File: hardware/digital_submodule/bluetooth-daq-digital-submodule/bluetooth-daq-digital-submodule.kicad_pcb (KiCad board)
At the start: 2 copper layers, 148 parts, among them J1 MCU I/F, J2 Digital Inputs, J3 Digital Outputs, J4 Communication I/F, J5 RS-485 I/F, U1 74HC595, U2 74HC595, U3 74HC165, U4 74HC165, U5 24LC1025, U6 SN75176AD, U7 CD4053B, U8 CD4053B

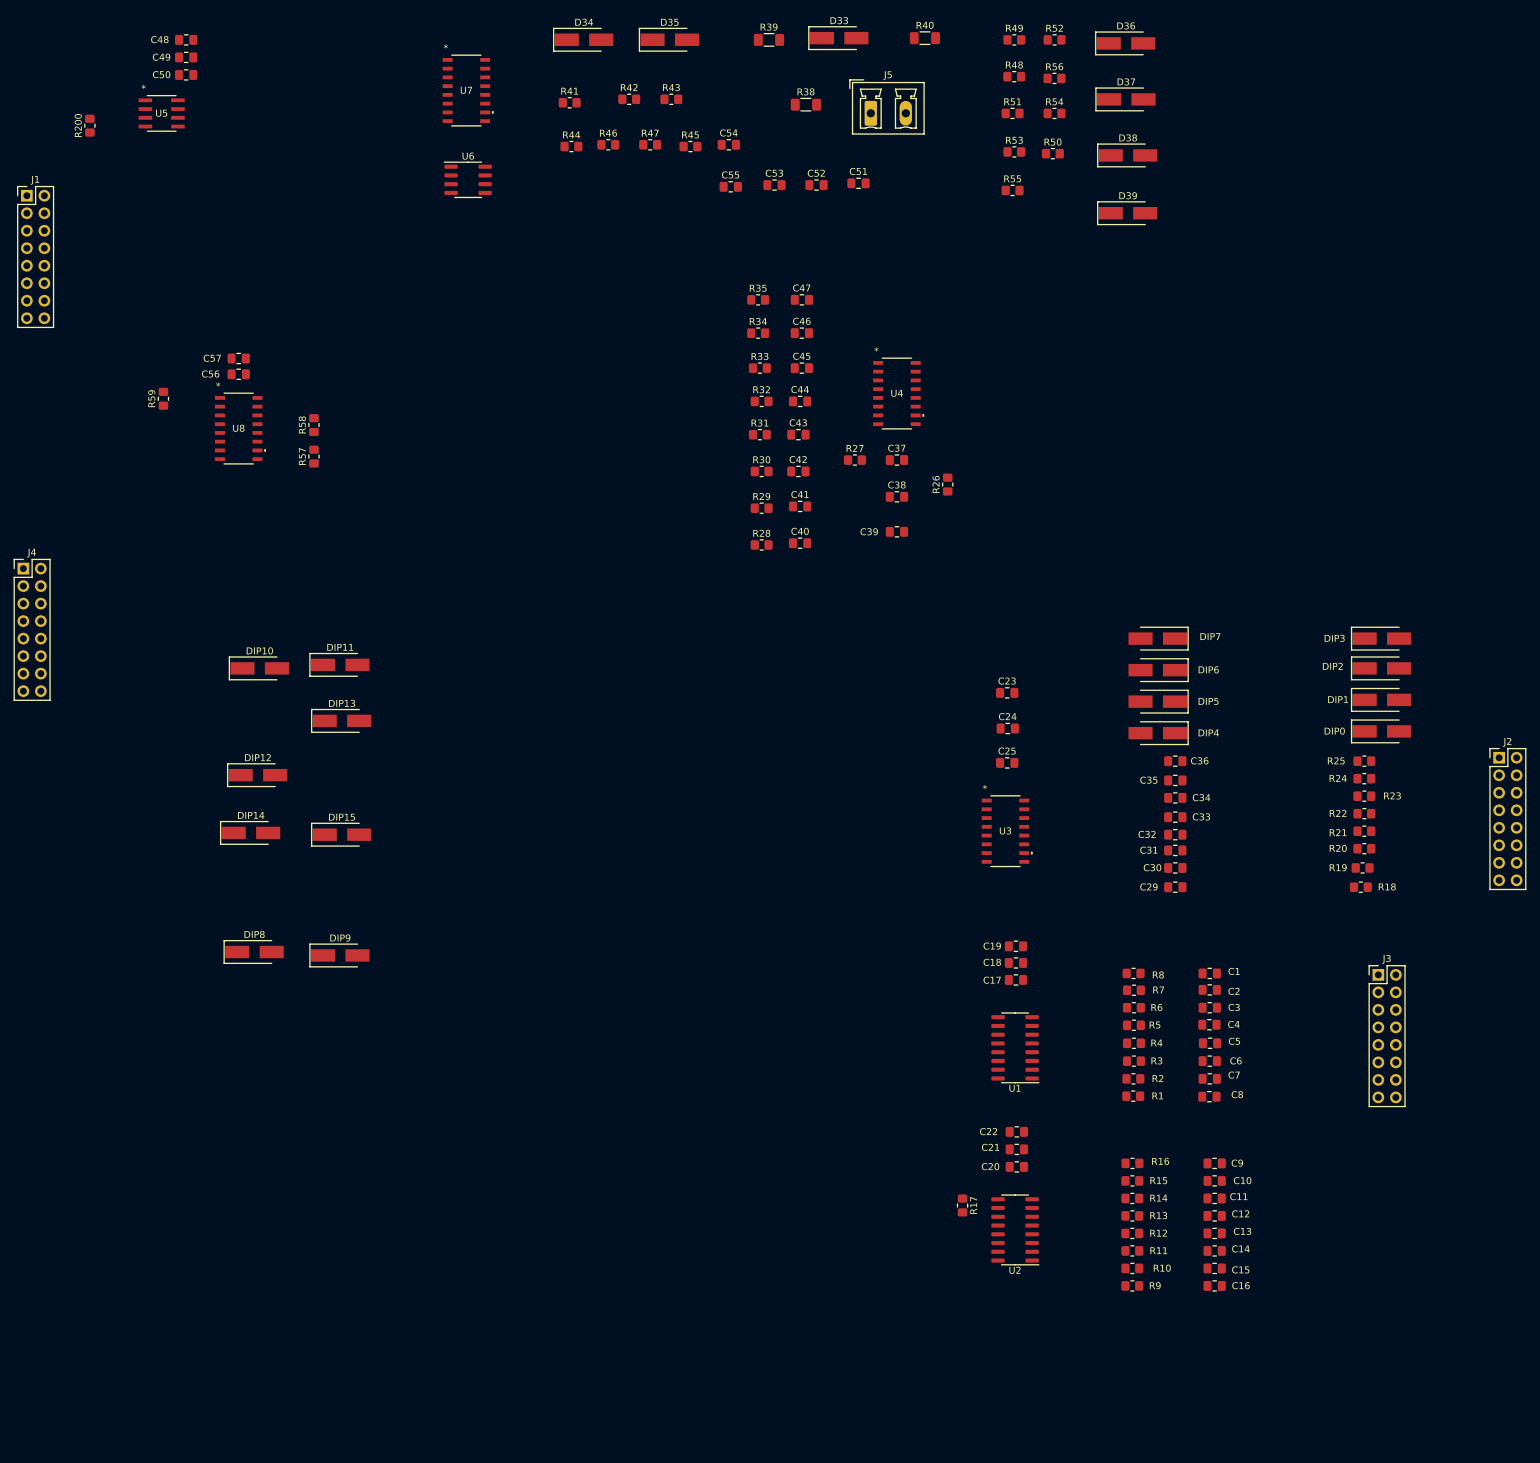
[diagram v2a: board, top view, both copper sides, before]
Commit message: Decided on initial component placement for digital submodule.
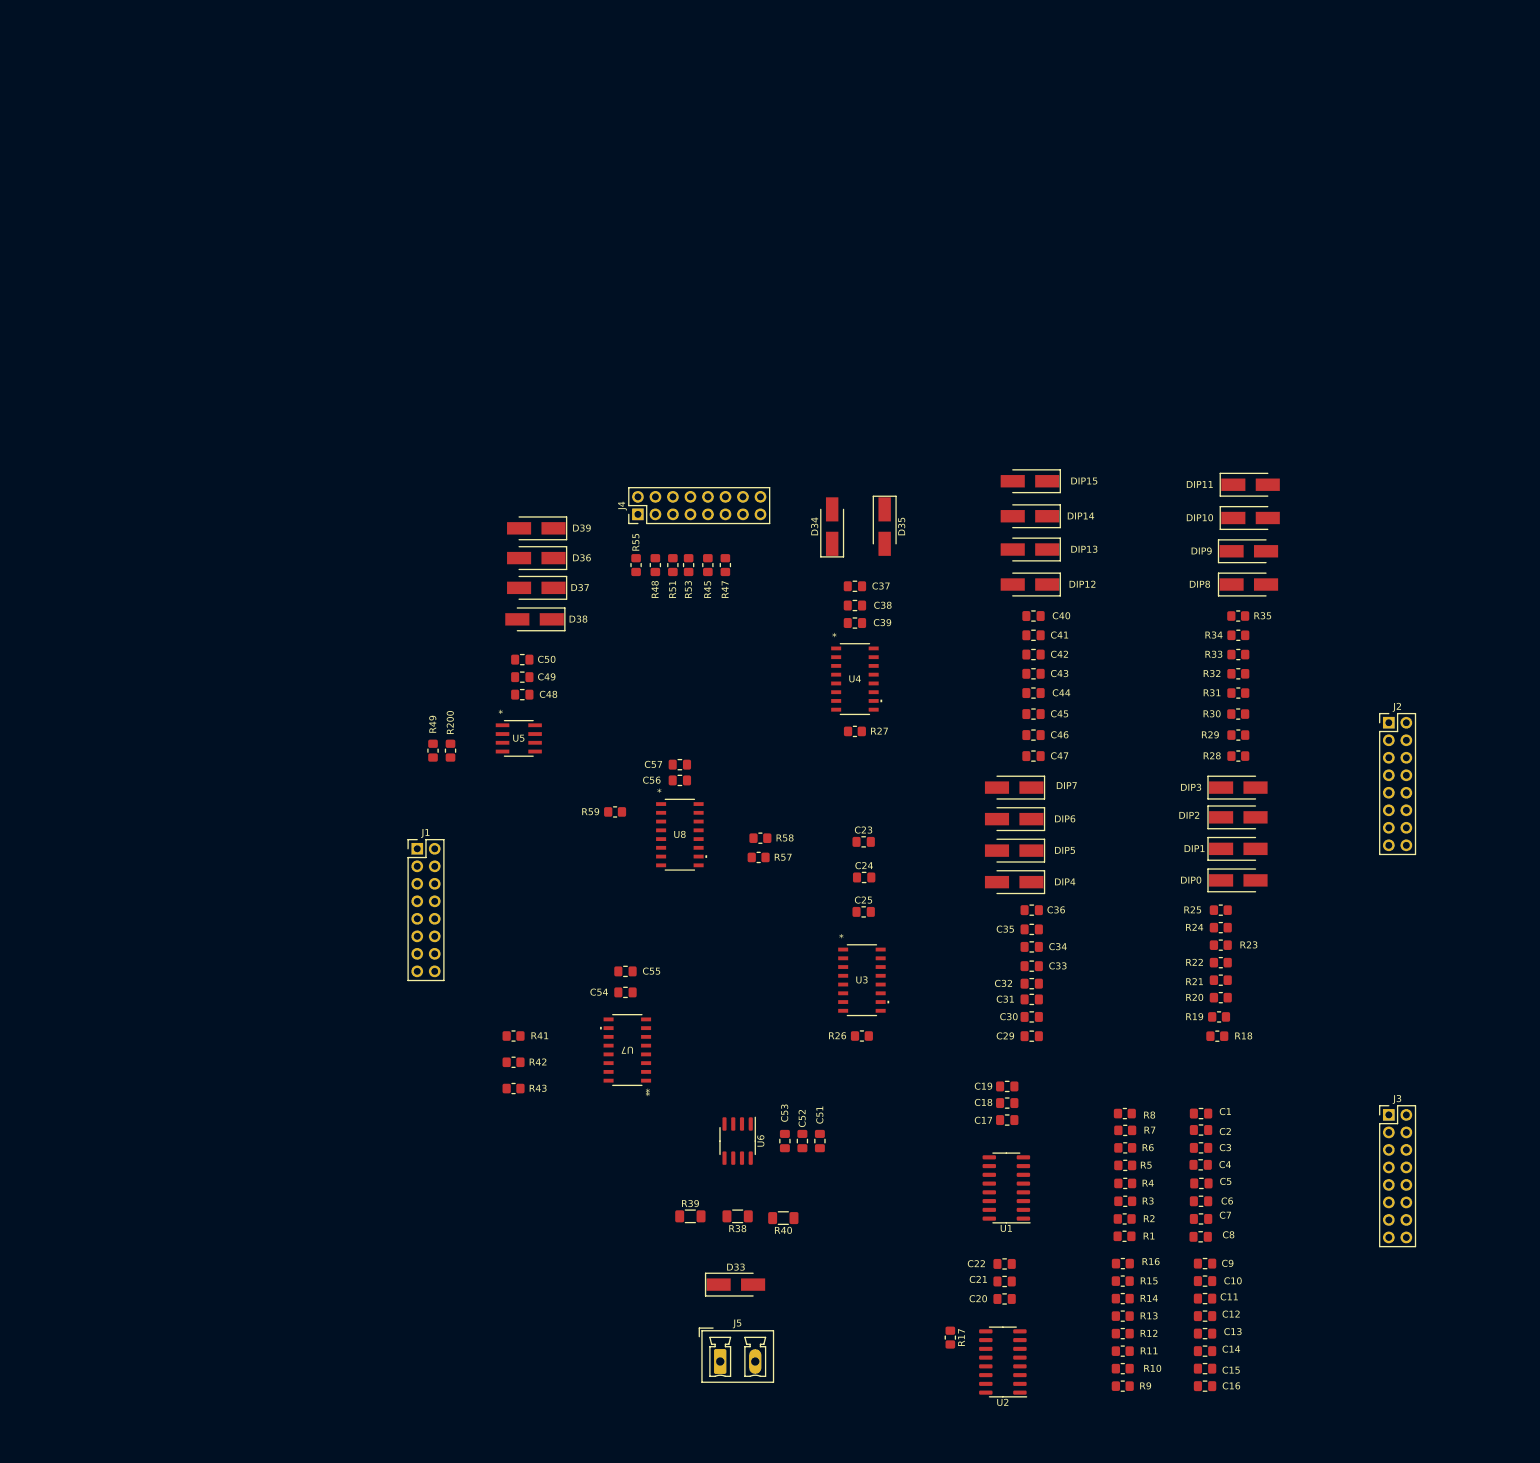
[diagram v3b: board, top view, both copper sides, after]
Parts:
- removed R44, R46: 33, Resistor_SMD:R_0805_2012Metric_Pad1.20x1.40mm_HandSolder
- removed R50, R52, R54, R56: 10, Resistor_SMD:R_0805_2012Metric_Pad1.20x1.40mm_HandSolder
- R48, R51, R53, R55: value 10 -> 22
- moved J5 182.4 mm to (130.3, 209.0)
- moved D33 181.5 mm to (132.6, 197.9)
- moved R40 172.4 mm to (139.5, 188.2), turned to 180 degrees
- moved R39 171.1 mm to (126.0, 188.0)
- moved R38 161.6 mm to (132.8, 188.0), turned to 180 degrees
- moved DIP8 153.8 mm to (207.0, 96.3)
- moved DIP10 145.4 mm to (207.3, 86.6)
- moved R43 145.3 mm to (100.3, 169.4), turned to 180 degrees
- moved U6 144.8 mm to (132.8, 177.0), turned to -90 degrees
- moved DIP9 144.3 mm to (207.0, 91.5)
- moved U7 141.2 mm to (116.8, 163.8), turned to 180 degrees
- moved R42 140.7 mm to (100.3, 165.6), turned to 180 degrees
- moved C51 139.1 mm to (144.8, 177.0), turned to 90 degrees
- moved C52 138.7 mm to (142.2, 177.0), turned to 90 degrees
- moved C53 138.7 mm to (139.7, 177.0), turned to 90 degrees
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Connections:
- D34 pad 1: Net-(R44-Pad2) -> Net-(D34-Pad1)
- D35 pad 2: Net-(R46-Pad2) -> Net-(D35-Pad2)
- D36 pad 1: Net-(D36-Pad1) -> XSPI_MISO
- D37 pad 1: Net-(D37-Pad1) -> XSPI_MOSI
- D38 pad 1: Net-(D38-Pad1) -> XSPI_SCLK
- D39 pad 1: Net-(D39-Pad1) -> XSPI_SEL_OUT
- J5 pad 1: Net-(U6-Pad7) -> Net-(U6-Pad6)
- J5 pad 2: Net-(U6-Pad6) -> Net-(U6-Pad7)
- R45 pad 1: Net-(R44-Pad2) -> Net-(D34-Pad1)
- R47 pad 1: Net-(R46-Pad2) -> Net-(D35-Pad2)
- R48 pad 2: Net-(D36-Pad1) -> XSPI_MISO
- R51 pad 2: Net-(D37-Pad1) -> XSPI_MOSI
- R53 pad 2: Net-(D38-Pad1) -> XSPI_SCLK
- R55 pad 2: Net-(D39-Pad1) -> XSPI_SEL_OUT
- U7 pad 1: Net-(U7-Pad1) -> Net-(D35-Pad2)
- U7 pad 13: Net-(U7-Pad13) -> Net-(D34-Pad1)

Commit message: Performed initial routing for digital submodule
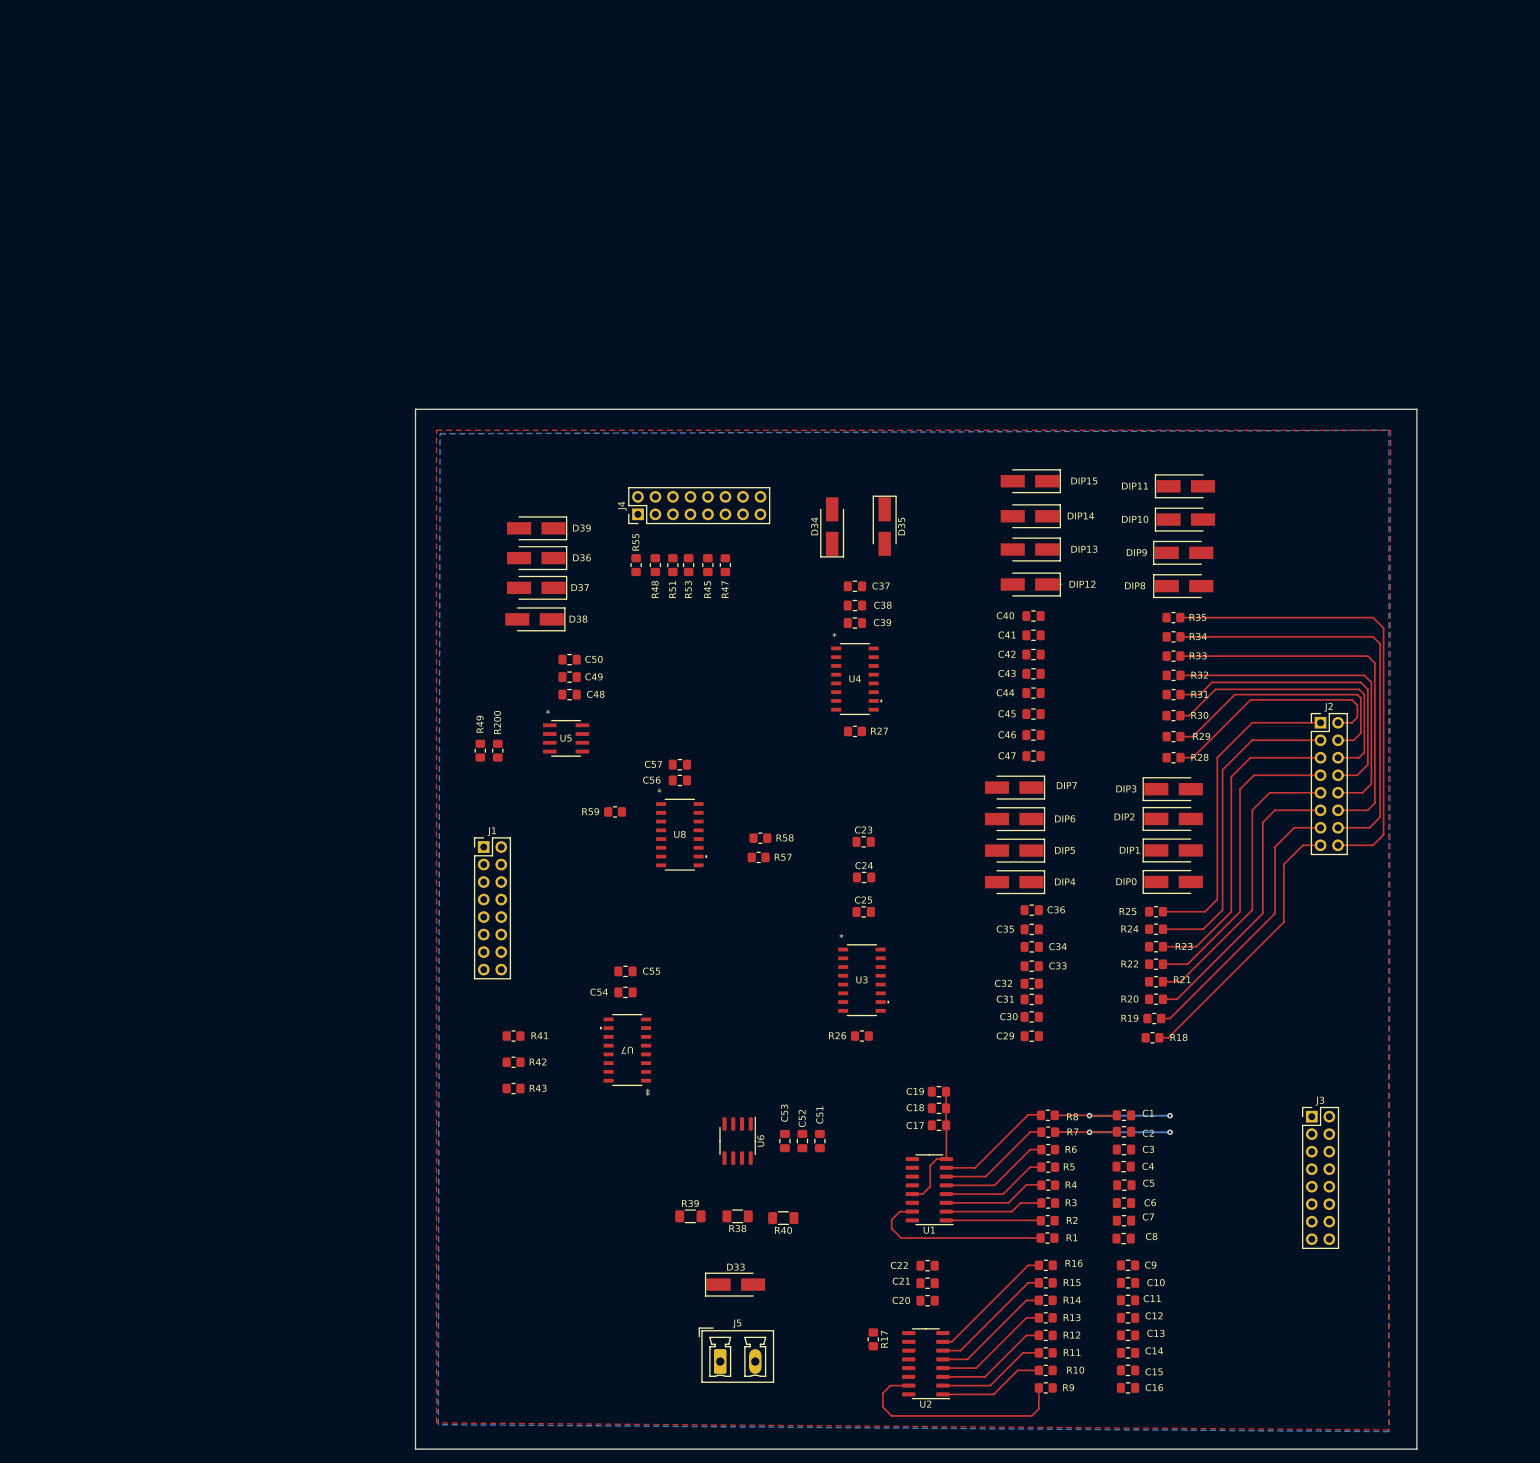
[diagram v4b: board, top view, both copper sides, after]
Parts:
- moved R10 11.2 mm to (177.5, 210.3)
- moved R13 11.2 mm to (177.5, 202.7)
- moved R17 11.2 mm to (152.5, 205.8)
- moved R8 11.2 mm to (177.9, 173.3)
- moved C4 11.2 mm to (188.8, 180.7)
- moved C8 11.2 mm to (188.8, 191.2)
- moved R11 11.2 mm to (177.5, 207.8)
- moved R12 11.2 mm to (177.5, 205.2)
- moved R14 11.2 mm to (177.5, 200.2)
- moved R15 11.2 mm to (177.5, 197.6)
- moved R9 11.2 mm to (177.5, 212.9)
- moved U2 11.2 mm to (160.1, 209.3)
- moved C1 11.2 mm to (188.9, 173.3)
- moved C12 11.2 mm to (189.5, 202.7)
- moved C15 11.2 mm to (189.5, 210.3)
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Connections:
- J2 pad 10: DIN12 -> DIN11
- J2 pad 12: DIN13 -> DIN10
- J2 pad 14: DIN14 -> DIN9
- J2 pad 16: DIN15 -> DIN8
- J2 pad 2: DIN8 -> DIN15
- J2 pad 4: DIN9 -> DIN14
- J2 pad 6: DIN10 -> DIN13
- J2 pad 8: DIN11 -> DIN12
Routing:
- net DIN8: track 0.00 -> 67.3 mm
- net DIN9: track 0.00 -> 61.3 mm
- net DIN10: track 0.00 -> 54.7 mm
- net DIN11: track 0.00 -> 48.2 mm
- net DIN0: track 0.00 -> 46.3 mm
- net DIN1: track 0.00 -> 46.1 mm
- net DIN2: track 0.00 -> 45.7 mm
- net DIN3: track 0.00 -> 44.6 mm
- net DIN12: track 0.00 -> 44.2 mm
- net DIN4: track 0.00 -> 42.7 mm
- net DIN5: track 0.00 -> 42.0 mm
- net DIN13: track 0.00 -> 41.1 mm
- net DIN6: track 0.00 -> 40.2 mm
- net DIN7: track 0.00 -> 39.9 mm
- net DIN14: track 0.00 -> 37.7 mm
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- added copper zone on F.Cu, net 3V3
- added copper zone on B.Cu, net GND
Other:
- board outline added: 145.3 x 150.9 mm

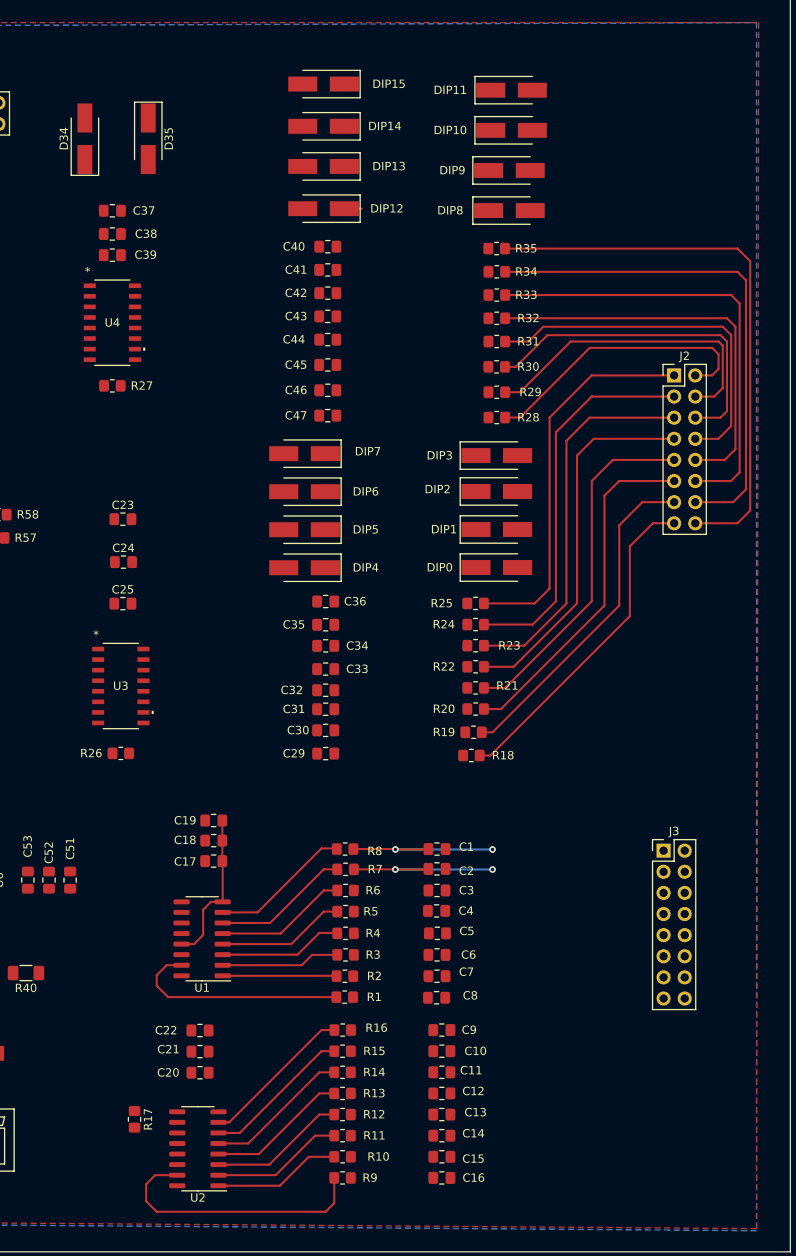
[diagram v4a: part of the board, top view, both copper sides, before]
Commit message: Routed digital output 1 of digital submodule
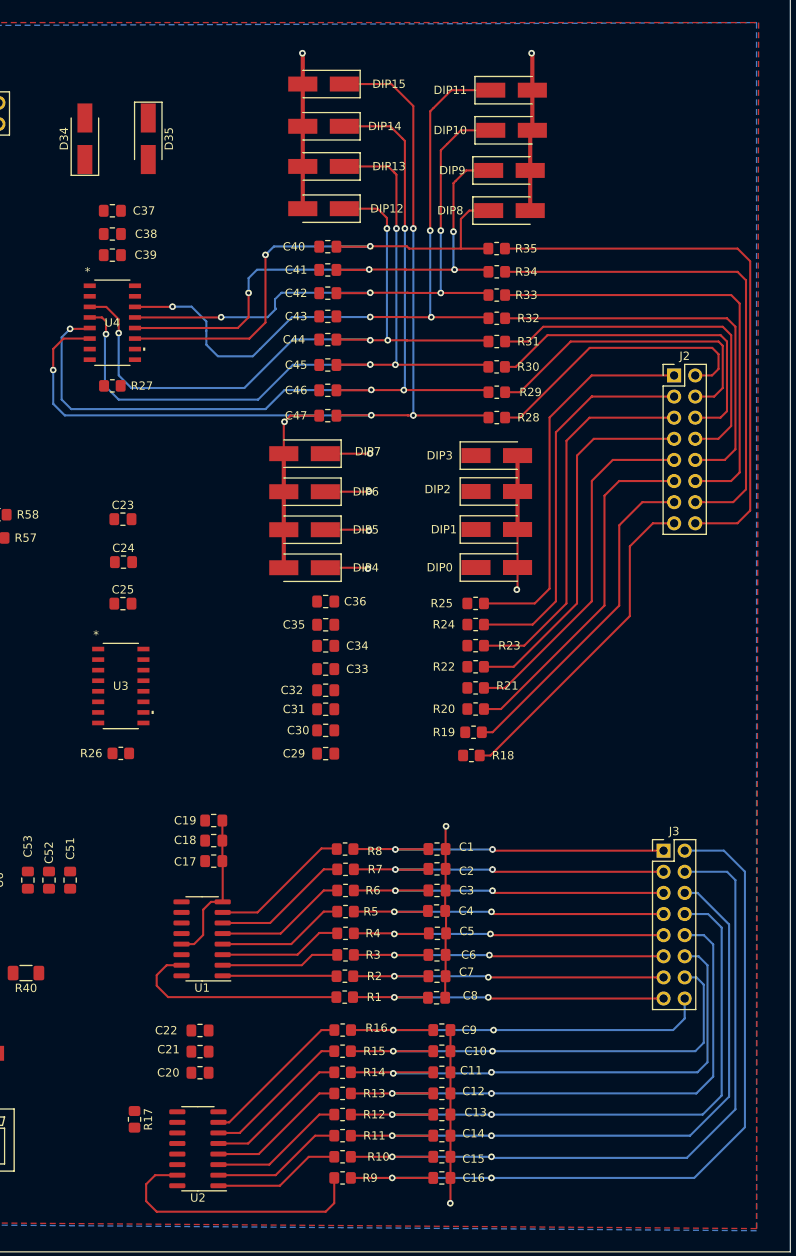
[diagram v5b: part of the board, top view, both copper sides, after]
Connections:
- J3 pad 10: DOUT11 -> DOUT12
- J3 pad 12: DOUT10 -> DOUT13
- J3 pad 14: DOUT9 -> DOUT14
- J3 pad 16: DOUT8 -> DOUT15
- J3 pad 2: DOUT15 -> DOUT8
- J3 pad 4: DOUT14 -> DOUT9
- J3 pad 6: DOUT13 -> DOUT10
- J3 pad 8: DOUT12 -> DOUT11
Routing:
- net GND: track 18.6 -> 136.2 mm, vias 0 -> 6
- net Net-(R28-Pad2): track 0.00 -> 115.8 mm, vias 0 -> 4
- net Net-(R29-Pad2): track 0.00 -> 106.4 mm, vias 0 -> 4
- net DOUT8: track 0.00 -> 93.9 mm, vias 0 -> 2
- net Net-(R30-Pad2): track 0.00 -> 92.3 mm, vias 0 -> 4
- net DOUT9: track 0.00 -> 87.7 mm, vias 0 -> 2
- net Net-(R32-Pad2): track 0.00 -> 81.9 mm, vias 0 -> 4
- net Net-(R31-Pad2): track 2.10 -> 83.2 mm, vias 0 -> 4
- net DOUT10: track 0.00 -> 80.0 mm, vias 0 -> 2
- net DOUT11: track 0.00 -> 75.8 mm, vias 0 -> 2
- net Net-(R33-Pad2): track 0.00 -> 73.1 mm, vias 0 -> 4
- net DOUT12: track 0.00 -> 69.1 mm, vias 0 -> 2
- net Net-(R34-Pad2): track 0.00 -> 67.6 mm, vias 0 -> 4
- net Net-(R35-Pad2): track 0.00 -> 63.7 mm, vias 0 -> 2
- net DOUT13: track 0.00 -> 63.2 mm, vias 0 -> 2
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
